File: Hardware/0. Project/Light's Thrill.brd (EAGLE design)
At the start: 42 x 32 mm, 39 parts, among them CN1 Micro-USB, CN2 2.1MMJACKTHM, Q1 SI2302DS, Q2 SI2302DS, Q3 SI2302DS, U1 TSOP1838, U2 ATMEGA32U4, U3 LM1117-5.0, Y1 16 MHz

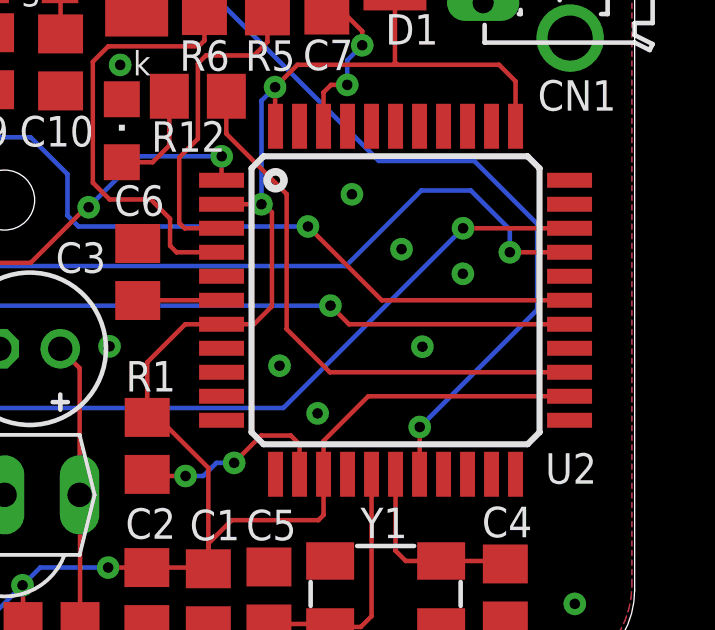
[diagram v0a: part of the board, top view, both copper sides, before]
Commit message: Schematic + PCB 1.3 up to date
- Change MCU_PWM_RED to a 16 bit PWM pin.
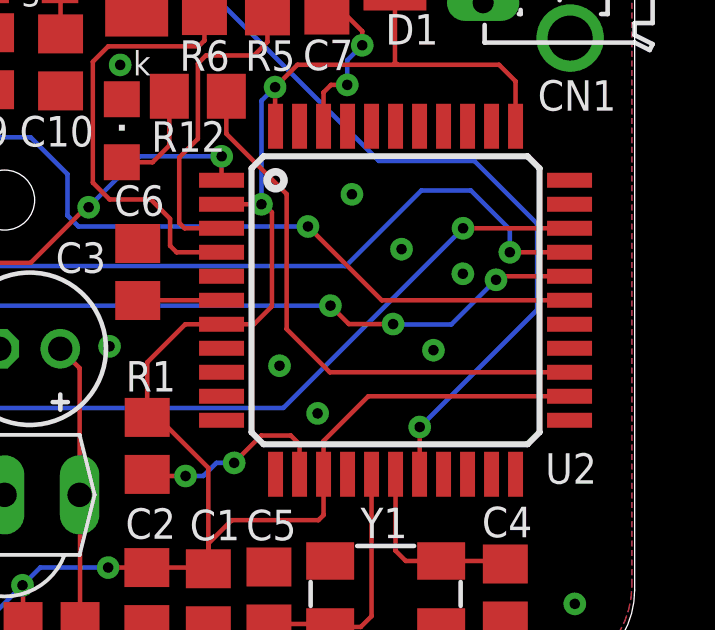
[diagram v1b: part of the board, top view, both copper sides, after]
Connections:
- net MCU_PWM_GREEN: now also U2.29; no longer U2.27
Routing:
- net MCU_PWM_GREEN: track 26.0 -> 26.6 mm, vias 2 -> 4
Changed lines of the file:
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@@
 </layers>
 <board>
-<fusionsync huburn="a.cGVyc29uYWw6dWUyOTAyNzk3" projecturn="a.cGVyc29uYWw6dWUyOTAyNzk3IzIwMjAwNzEyMzE1MDYxNTUx" f3durn="urn:adsk.wipprod:dm.lineage:tlLarB8OSj-ZujroCSfv0w" pcbguid="" lastpulledtime="" lastsyncedchangeguid="" latestrevisionid="f68e5461-e1b2-4b56-a579-d7a7db826cba" lastsyncedrevisionid="f68e5461-e1b2-4b56-a579-d7a7db826cba" lastboardhashguid="fa5e43d7-5d8a-6991-a6be-681723860f97" lastpushedtime="2020-07-12T21:20:11Z" linktopcb3d="true"/>
+<fusionsync huburn="a.cGVyc29uYWw6dWUyOTAyNzk3" projecturn="a.cGVyc29uYWw6dWUyOTAyNzk3IzIwMjAwNzEyMzE1MDYxNTUx" f3durn="urn:adsk.wipprod:dm.lineage:tlLarB8OSj-ZujroCSfv0w" pcbguid="" lastpulledtime="" lastsyncedchangeguid="" latestrevisionid="f68e5461-e1b2-4b56-a579-d7a7db826cba" lastsyncedrevisionid="f68e5461-e1b2-4b56-a579-d7a7db826cba" lastboardhashguid="fa5e43d7-5d8a-6991-a6be-681723860f97" lastpushedtime="2020-07-12T21:20:11Z" linktopcb3d="false"/>
 <plain>
 <hole x="21" y="16" drill="2" locked="yes"/>
@@
 <via x="30.1625" y="10.4775" extent="1-16" drill="0.35"/>
 <via x="31.4325" y="8.89" extent="1-16" drill="0.35"/>
-<via x="34.925" y="11.1125" extent="1-16" drill="0.35"/>
+<via x="35.2933" y="10.9956625" extent="1-16" drill="0.35"/>
 <via x="40.005" y="2.54" extent="1-16" drill="0.35"/>
 <via x="7.3025" y="1.5875" extent="1-16" drill="0.35"/>
@@
 </signal>
 <signal name="MCU_PWM_GREEN">
-<contactref element="U2" pad="27"/>
 <contactref element="R7" pad="1"/>
 <wire x1="16.13664375" y1="12.64005625" x2="16.22" y2="12.5567" width="0.1524" layer="1"/>
@@
 <wire x1="17.52" y1="12.48" x2="31.86" y2="12.48" width="0.1524" layer="16"/>
 <via x="31.86" y="12.48" extent="1-16" drill="0.35"/>
-<wire x1="39.83" y1="11.86" x2="32.48" y2="11.86" width="0.1524" layer="1"/>
-<wire x1="32.48" y1="11.86" x2="31.86" y2="12.48" width="0.1524" layer="1"/>
+<contactref element="U2" pad="29"/>
+<wire x1="31.86" y1="12.48" x2="32.47311875" y2="11.86688125" width="0.1524" layer="1"/>
+<wire x1="39.83" y1="13.46" x2="37.496021875" y2="13.46" width="0.1524" layer="1"/>
+<wire x1="37.496021875" y1="13.46" x2="37.378640625" y2="13.34261875" width="0.1524" layer="1"/>
+<via x="37.378640625" y="13.34261875" extent="1-16" drill="0.35"/>
+<wire x1="37.378640625" y1="13.34261875" x2="35.890203125" y2="11.85418125" width="0.1524" layer="16"/>
+<wire x1="35.890203125" y1="11.85418125" x2="33.9471" y2="11.85418125" width="0.1524" layer="16"/>
+<wire x1="33.9471" y1="11.85418125" x2="33.9471" y2="11.86688125" width="0.1524" layer="16"/>
+<via x="33.9471" y="11.86688125" extent="1-16" drill="0.35"/>
+<wire x1="32.47311875" y1="11.86688125" x2="33.9471" y2="11.86688125" width="0.1524" layer="1"/>
 </signal>
 <signal name="N$5">

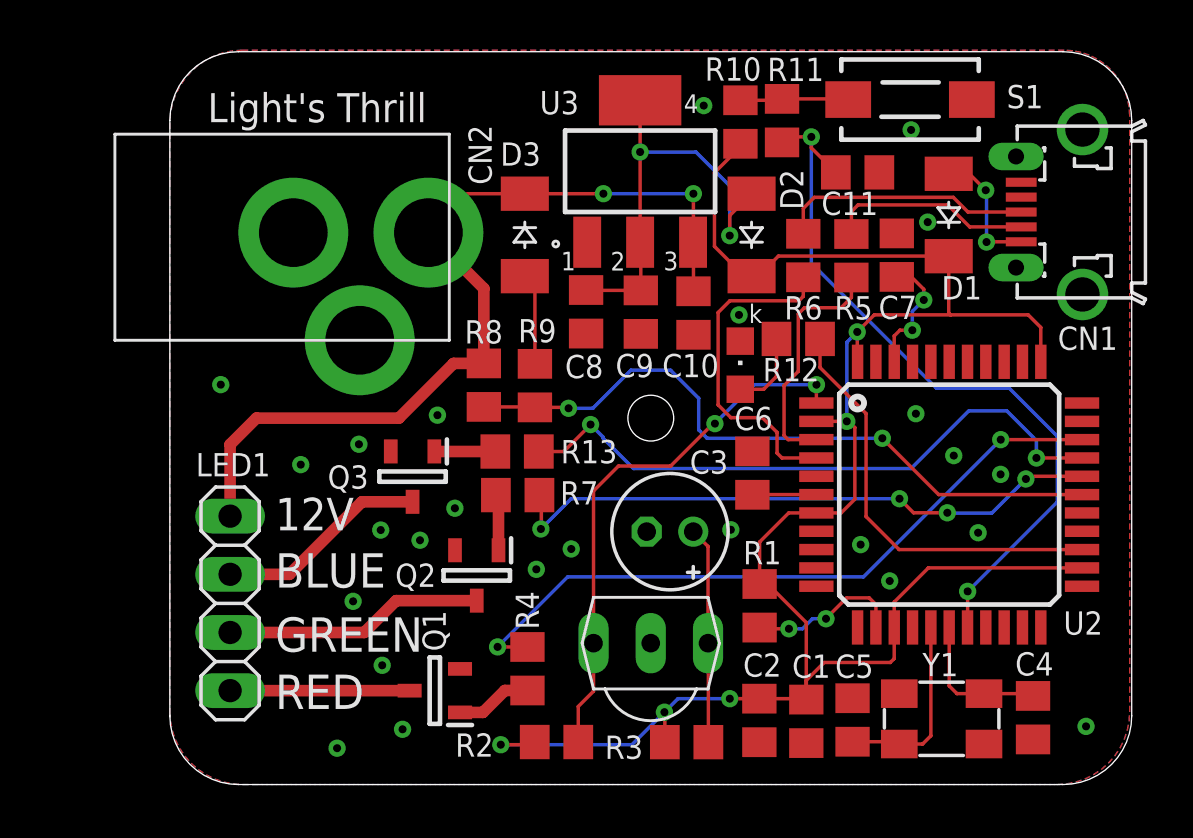
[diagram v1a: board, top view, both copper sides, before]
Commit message: ICSP Programming added (PCB 1.4)
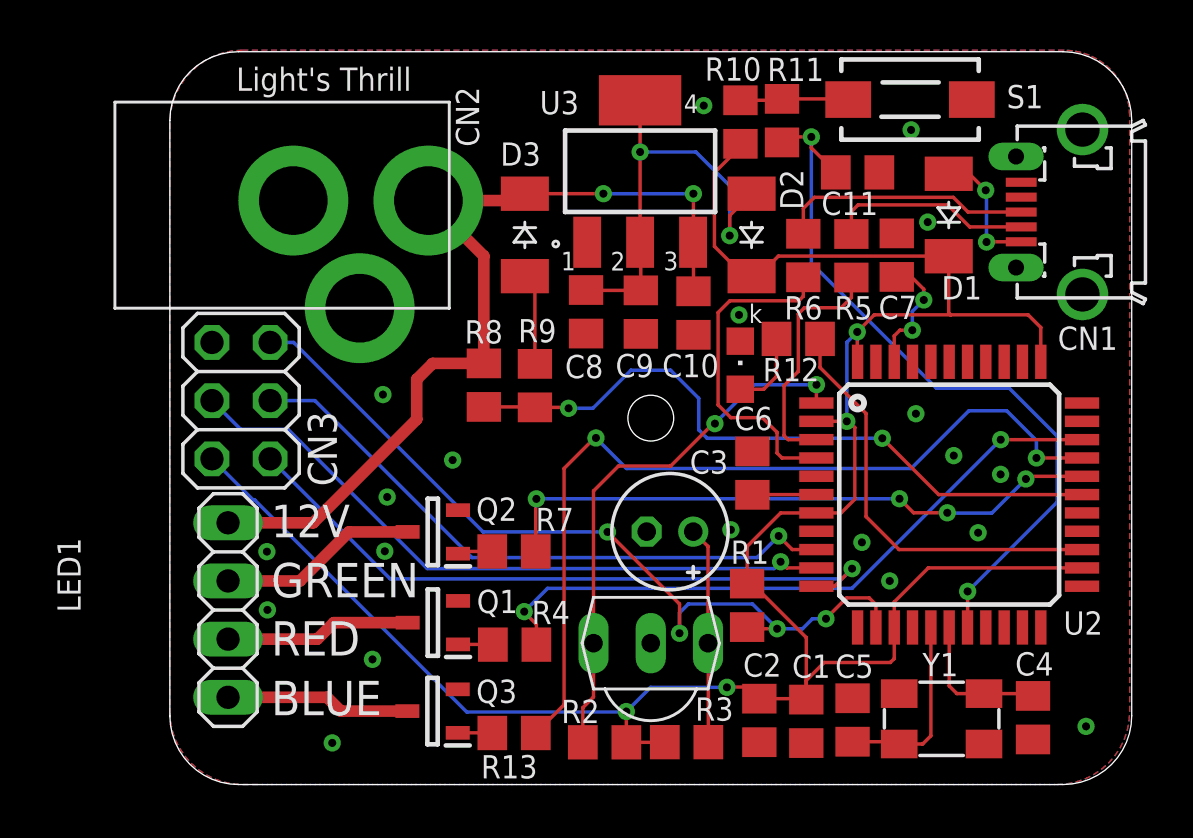
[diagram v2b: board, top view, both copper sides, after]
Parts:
- added CN3: 2x3, pinhead:2X03
- LED2: value (none) -> Red
- moved R13 12.3 mm to (15.0, 2.25)
- moved Q3 10.3 mm to (11.5, 3.21), turned to 180 degrees
- moved Q1 2.97 mm to (11.5, 7.07)
- moved Q2 2.70 mm to (11.5, 11.0), turned to 180 degrees
- moved R7 2.47 mm to (15.0, 10.2)
- moved R2 2.10 mm to (19.0, 1.84), turned to 180 degrees
- moved CN2 1.40 mm to (2.00, 25.4)
- moved R4 1.19 mm to (15.1, 6.11), turned to 180 degrees
- moved R1 0.54 mm to (25.2, 7.83)
- moved LED1 0.30 mm to (2.54, 7.62)
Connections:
- removed net N$10: R1.1, U2.13
- new net ICSP_MISO: CN3.1, U2.11
- new net ICSP_MOSI: CN3.4, U2.10
- new net ICSP_RESET: CN3.5, R1.1, U2.13
- new net ICSP_SCK: CN3.3, U2.9
- net +5V: now also CN3.2
- net GND: now also CN3.6
- net N$2: now also LED1.3; no longer LED1.4
- net N$5: now also LED1.2; no longer LED1.3
- net N$6: now also LED1.4; no longer LED1.2
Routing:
- net ICSP_RESET: track 0.00 -> 37.0 mm, vias 0 -> 4
- net ICSP_MOSI: track 0.00 -> 29.7 mm, vias 0 -> 1
- net ICSP_MISO: track 0.00 -> 29.6 mm, vias 0 -> 1
- net ICSP_SCK: track 0.00 -> 27.3 mm, vias 0 -> 1
- net +5V: track 85.3 -> 103.1 mm, vias 5 -> 4
- net MCU_PWM_BLUE: track 27.4 -> 38.1 mm
- net N$10: track 6.78 -> 0.00 mm, vias 2 -> 0
- net N$5: track 11.3 -> 8.73 mm
- net N$1: track 3.34 -> 1.52 mm
- net MCU_PWM_RED: track 30.6 -> 29.1 mm
- net N$6: track 9.28 -> 8.08 mm
- net N$4: track 2.66 -> 1.51 mm
- net N$3: track 2.46 -> 1.53 mm
- net GND: vias 25 -> 20
